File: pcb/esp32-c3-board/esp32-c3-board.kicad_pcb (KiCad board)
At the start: 2 copper layers, 118.7 x 40.6 mm, 30 parts, among them P101 CAN, P102 RS485, P3 CONN_1, P4 CONN_1, P5 CONN_1, P6 CONN_1, U102 TJA1050, U2 esp32-c3-ebay, U4 6N137, U5 DCDCConverter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

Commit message: Updated boards and readme
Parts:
- moved R3 1.20 mm to (116.1, 58.7)
- moved R4 0.81 mm to (101.1, 64.8)
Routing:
- net 3v3: track 24.9 -> 26.8 mm
- net GND: track 177.3 -> 176.3 mm
- net Net-(U4-A): track 2.93 -> 3.91 mm
- net 5V BMS: track 24.8 -> 25.6 mm
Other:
- board text added: "BMS Uart"
- board text removed: "MBS Uart"

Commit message: messed up bms uart connector
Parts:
- P102: value RS485 -> BMS UART
- R3: value 4K7 -> 2K2
- R4: value 3K3 -> 1K
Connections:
- P102 pad 2: RX from BMS -> TX to BMS
- P102 pad 3: TX to BMS -> RX from BMS
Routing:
- net Net-(U4-A): track 3.91 -> 13.7 mm
- net RX from BMS: track 22.8 -> 14.7 mm
- net 5V BMS: track 25.6 -> 31.1 mm
- net TX to BMS: track 15.7 -> 14.7 mm
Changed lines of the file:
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@@
         (effects (font (size 1 1) (thickness 0.15)))
     )
-    (fp_text value "RS485" (at 3.75 10.4 90) (layer "F.Fab")
+    (fp_text value "BMS UART" (at 3.75 10.4 90) (layer "F.Fab")
         (effects (font (size 1 1) (thickness 0.15)))
     )
@@
     (fp_line (start 9.95 9.2) (end 9.95 -2.3)
       (stroke (width 0.1) (type solid)) (layer "F.Fab"))
-    (pad "1" thru_hole roundrect (at 0 0 90) (size 2 2.5) (drill 0.95) (layers "*.Cu" "*.Mask") (roundrect_rratio 0.147059)
+    (pad "1" thru_hole roundrect (at 0 0 90) (size 2 5) (drill 0.95) (layers "*.Cu" "*.Mask") (roundrect_rratio 0.147059)
       (net 2 "GND BMS") (pinfunction "P1") (pintype "passive"))
-    (pad "2" thru_hole oval (at 2.5 0 90) (size 2 2.5) (drill 0.95) (layers "*.Cu" "*.Mask")
-      (net 14 "RX from BMS") (pinfunction "P2") (pintype "passive"))
-    (pad "3" thru_hole oval (at 5 0 90) (size 2 2.5) (drill 0.95) (layers "*.Cu" "*.Mask")
-      (net 3 "TX to BMS") (pinfunction "P3") (pintype "passive"))
-    (pad "4" thru_hole oval (at 7.5 0 90) (size 2 2.5) (drill 0.95) (layers "*.Cu" "*.Mask")
+    (pad "2" thru_hole oval (at 2.5 0 90) (size 2 5) (drill 0.95) (layers "*.Cu" "*.Mask")
+      (net 3 "TX to BMS") (pinfunction "P2") (pintype "passive"))
+    (pad "3" thru_hole oval (at 5 0 90) (size 2 5) (drill 0.95) (layers "*.Cu" "*.Mask")
+      (net 14 "RX from BMS") (pinfunction "P3") (pintype "passive"))
+    (pad "4" thru_hole oval (at 7.5 0 90) (size 2 5) (drill 0.95) (layers "*.Cu" "*.Mask")
       (net 1 "5V BMS") (pinfunction "P4") (pintype "passive"))
     (model "${KICAD6_3DMODEL_DIR}/Connector_JST.3dshapes/JST_XH_S4B-XH-A_1x04_P2.50mm_Horizontal.wrl"
@@
         (effects (font (size 1 1) (thickness 0.15)))
     )
-    (fp_text value "4K7" (at 0 1.65 90) (layer "F.Fab")
+    (fp_text value "2K2" (at 0 1.65 90) (layer "F.Fab")
         (effects (font (size 1 1) (thickness 0.15)))
     )
@@
         (effects (font (size 1 1) (thickness 0.15)))
     )
-    (fp_text value "3K3" (at 0 1.65 90) (layer "F.Fab")
+    (fp_text value "1K" (at 0 1.65 90) (layer "F.Fab")
         (effects (font (size 1 1) (thickness 0.15)))
     )
@@
   (segment (start 110.744 63.5) (end 110.0875 64.1565) (width 1) (layer "F.Cu") (net 1))
   (segment (start 112.405 63.347) (end 116.078 59.674) (width 1) (layer "F.Cu") (net 1))
-  (segment (start 118.446522 60.055) (end 120.596522 57.905) (width 1) (layer "F.Cu") (net 1))
   (segment (start 111.899416 63.51) (end 111.889416 63.5) (width 1) (layer "F.Cu") (net 1))
-  (segment (start 118.446522 60.055) (end 116.459 60.055) (width 1) (layer "F.Cu") (net 1))
   (segment (start 110.0875 64.1565) (end 110.0875 74.295) (width 1) (layer "F.Cu") (net 1))
-  (segment (start 120.596522 57.905) (end 122.555 57.905) (width 1) (layer "F.Cu") (net 1))
+  (segment (start 112.405 63.51) (end 118.01 57.905) (width 1) (layer "B.Cu") (net 1))
+  (segment (start 118.01 57.905) (end 122.555 57.905) (width 1) (layer "B.Cu") (net 1))
   (segment (start 114.935 70.8875) (end 117.0725 70.8875) (width 1) (layer "F.Cu") (net 2))
   (segment (start 114.6925 71.13) (end 114.935 70.8875) (width 1) (layer "F.Cu") (net 2))
@@
   (segment (start 112.405 71.13) (end 112.405 74.0525) (width 1) (layer "F.Cu") (net 2))
   (segment (start 112.405 68.59) (end 114.7125 68.59) (width 1) (layer "F.Cu") (net 3))
-  (segment (start 114.935 65.405) (end 119.935 60.405) (width 1) (layer "F.Cu") (net 3))
-  (segment (start 119.935 60.405) (end 122.555 60.405) (width 1) (layer "F.Cu") (net 3))
+  (segment (start 123.23 62.23) (end 122.555 62.905) (width 1) (layer "F.Cu") (net 3))
+  (segment (start 119.055 62.905) (end 114.935 67.025) (width 1) (layer "F.Cu") (net 3))
+  (segment (start 122.555 62.905) (end 119.055 62.905) (width 1) (layer "F.Cu") (net 3))
   (segment (start 114.7125 68.59) (end 114.935 68.8125) (width 1) (layer "F.Cu") (net 3))
-  (segment (start 114.935 68.8125) (end 114.935 65.405) (width 1) (layer "F.Cu") (net 3))
+  (segment (start 114.935 67.025) (end 114.935 68.8125) (width 1) (layer "F.Cu") (net 3))
   (segment (start 67.31 46.99) (end 68.81 45.49) (width 2) (layer "F.Cu") (net 4))
   (segment (start 38.8376 72.2874) (end 38.1 73.025) (width 1) (layer "F.Cu") (net 4))
@@
   (segment (start 40.145 62.23) (end 36.353 62.23) (width 1) (layer "F.Cu") (net 13))
   (segment (start 36.353 62.23) (end 34.6456 63.9374) (width 1) (layer "F.Cu") (net 13))
-  (segment (start 124.46 54.61) (end 125.095 55.245) (width 1) (layer "F.Cu") (net 14))
-  (segment (start 123.23 62.23) (end 122.555 62.905) (width 1) (layer "F.Cu") (net 14))
-  (segment (start 112.385 54.6) (end 121.91 54.6) (width 1) (layer "F.Cu") (net 14))
-  (segment (start 125.095 62.23) (end 123.23 62.23) (width 1) (layer "F.Cu") (net 14))
-  (segment (start 125.095 55.245) (end 125.095 62.23) (width 1) (layer "F.Cu") (net 14))
-  (segment (start 121.91 54.6) (end 121.92 54.61) (width 1) (layer "F.Cu") (net 14))
-  (segment (start 121.92 54.61) (end 124.46 54.61) (width 1) (layer "F.Cu") (net 14))
+  (segment (start 119.055 60.405) (end 122.555 60.405) (width 1) (layer "F.Cu") (net 14))
+  (segment (start 116.83 54.6) (end 118.11 55.88) (width 1) (layer "F.Cu") (net 14))
+  (segment (start 112.385 54.6) (end 116.83 54.6) (width 1) (layer "F.Cu") (net 14))
+  (segment (start 118.11 55.88) (end 118.11 59.46) (width 1) (layer "F.Cu") (net 14))
+  (segment (start 118.11 59.46) (end 119.055 60.405) (width 1) (layer "F.Cu") (net 14))
   (segment (start 78.63 61.595) (end 72.755 61.595) (width 1) (layer "F.Cu") (net 15))
   (segment (start 72.755 61.595) (end 68.945 65.405) (width 1) (layer "F.Cu") (net 15))
   (segment (start 68.945 65.405) (end 68.945 67.31) (width 1) (layer "F.Cu") (net 15))
   (segment (start 66.945 65.405) (end 61.53 65.405) (width 1) (layer "F.Cu") (net 16))
+  (segment (start 110.48 57.14) (end 109.982 56.642) (width 1) (layer "F.Cu") (net 17))
+  (segment (start 109.982 56.642) (end 109.982 51.308) (width 1) (layer "F.Cu") (net 17))
   (segment (start 115.544 57.14) (end 116.078 57.674) (width 1) (layer "F.Cu") (net 17))
   (segment (start 112.385 57.14) (end 115.544 57.14) (width 1) (layer "F.Cu") (net 17))
+  (segment (start 109.982 51.308) (end 111.252 50.038) (width 1) (layer "F.Cu") (net 17))
+  (segment (start 112.385 57.14) (end 110.48 57.14) (width 1) (layer "F.Cu") (net 17))
   (segment (start 101.092 65.77) (end 104.505 65.77) (width 1) (layer "F.Cu") (net 18))
   (segment (start 104.505 65.77) (end 104.785 66.05) (width 1) (layer "F.Cu") (net 18))
@@
   (segment (start 78.63 56.515) (end 79.53 56.515) (width 1) (layer "F.Cu") (net 28))
   (zone (net 4) (net_name "GND") (layers "F&B.Cu") (hatch edge 0.5)
-    (connect_pads (clearance 0.5))
-    (min_thickness 0.5) (filled_areas_thickness no)
-    (fill yes (thermal_gap 0.5) (thermal_bridge_width 0.5) (smoothing fillet) (radius 1))
+    (connect_pads yes (clearance 1))
+    (min_thickness 1) (filled_areas_thickness no)
+    (fill yes (thermal_gap 1) (thermal_bridge_width 1) (smoothing fillet) (radius 1))
     (polygon
       (pts
@@
   (zone (net 2) (net_name "GND BMS") (layers "F&B.Cu") (hatch edge 0.5)
     (priority 1)
-    (connect_pads (clearance 0.5))
+    (connect_pads yes (clearance 1))
     (min_thickness 0.5) (filled_areas_thickness no)
     (fill yes (thermal_gap 0.5) (thermal_bridge_width 0.5) (smoothing fillet) (radius 1))

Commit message: Working version connected to real BMS
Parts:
- removed C1, C4: 100nF, Capacitor_SMD:C_0805_2012Metric_Pad1.18x1.45mm_HandSolder
- removed C2, C3: 15pF, Capacitor_SMD:C_0805_2012Metric_Pad1.18x1.45mm_HandSolder
- removed R3: 2K2, Resistor_SMD:R_0805_2012Metric_Pad1.20x1.40mm_HandSolder
- removed R4: 1K, Resistor_SMD:R_0805_2012Metric_Pad1.20x1.40mm_HandSolder
- removed U6: 6N137, Package_DIP:DIP-8_W7.62mm
- added C5: 10uF, Capacitor_SMD:C_0805_2012Metric_Pad1.18x1.45mm_HandSolder, F.Cu at (112.4, 57.1)
- added C6: 10nF, Capacitor_SMD:C_0805_2012Metric_Pad1.18x1.45mm_HandSolder, F.Cu at (112.4, 55.1)
- added C7: 10uF, Capacitor_SMD:C_0805_2012Metric_Pad1.18x1.45mm_HandSolder, F.Cu at (118.1, 47.0)
- added R6: 3K3, Resistor_SMD:R_0805_2012Metric_Pad1.20x1.40mm_HandSolder, F.Cu at (115.1, 45.9)
- added R7: 10K, Resistor_SMD:R_0805_2012Metric_Pad1.20x1.40mm_HandSolder, F.Cu at (115.1, 43.4)
- added R8: 10K, Resistor_SMD:R_0805_2012Metric_Pad1.20x1.40mm_HandSolder, F.Cu at (98.6, 48.7)
- added U3: LP2985-3.3, Package_TO_SOT_SMD:SOT-23-5, F.Cu at (116.3, 51.6)
- added U7: STIS0621, Package_SO:SOIC-8_3.9x4.9mm_P1.27mm, F.Cu at (107.6, 62.9)
- U4: value 6N137 -> PC817; footprint Package_DIP:DIP-8_W7.62mm -> Package_DIP:DIP-4_W7.62mm
- moved U4 18.2 mm to (104.2, 43.5), turned to 0 degrees
- moved TH201 0.56 mm to (47.0, 53.9)
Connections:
- net Net-(D203-K) renamed 12vFused
- P102 pad 4: 5V BMS -> 12V BMS
- U4 pad 1: unconnected-(U4-NC-Pad1) -> Net-(R8-Pad1)
- U4 pad 2: Net-(U4-A) -> GND
- U4 pad 3: RX from BMS -> Net-(U3-ON/~{OFF})
- U4 pad 4: (no net) -> Net-(R7-Pad1)
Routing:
- net GND BMS: track 15.8 -> 58.3 mm, vias 0 -> 2
- net GND: track 176.3 -> 218.2 mm, vias 0 -> 1
- net 12V BMS: track 0.00 -> 31.2 mm
- net 5V BMS: track 31.1 -> 0.00 mm
- net 3v3: track 26.8 -> 9.08 mm, vias 1 -> 0
- net 3.3V BMS: track 0.00 -> 14.3 mm
- net Net-(U4-A): track 13.7 -> 0.00 mm
- net Net-(R8-Pad1): track 0.00 -> 8.12 mm
- net Net-(U3-ON/~{OFF}): track 0.00 -> 7.36 mm
- net BMS-RX: track 14.3 -> 9.46 mm
- net Net-(U3-BP): track 0.00 -> 3.96 mm
- net Net-(U6-A): track 3.81 -> 0.00 mm
- net Net-(R7-Pad1): track 0.00 -> 2.31 mm
- net TX to BMS: track 14.7 -> 12.8 mm
- net 12v: track 5.31 -> 7.06 mm
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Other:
- board text added: "BMS 0V"
- board text added: "BMS 12V"
- board text added: "RX"
- board text added: "TX"
- board text removed: "BMS Uart"

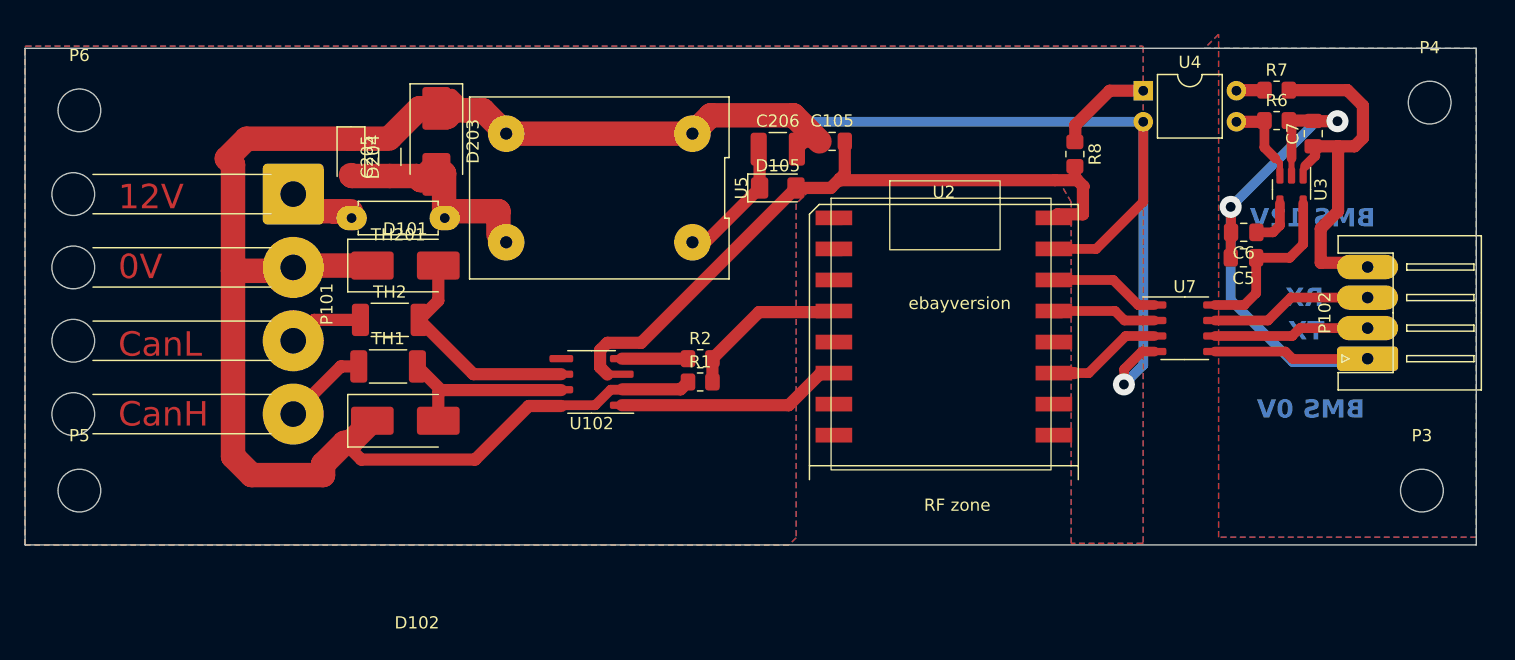
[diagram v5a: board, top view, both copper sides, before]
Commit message: Added engine Freeze frame functoinality
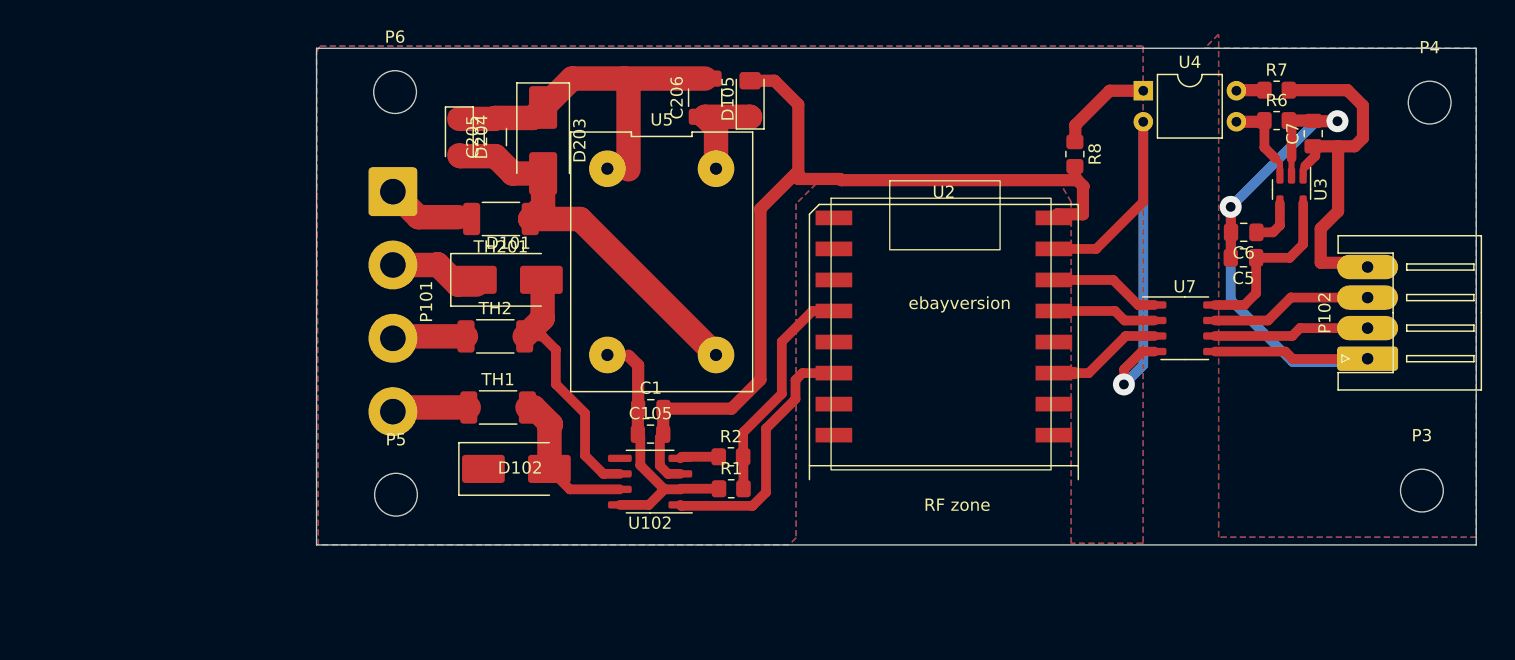
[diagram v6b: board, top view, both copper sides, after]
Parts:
- added C1: 10uF, Capacitor_SMD:C_0805_2012Metric_Pad1.18x1.45mm_HandSolder, F.Cu at (63.9, 69.5)
- P101: footprint Connector_Wire:SolderWire-1.5sqmm_1x04_P6mm_D1.7mm_OD3mm_Relief -> Connector_Wire:SolderWire-1.5sqmm_1x04_P6mm_D1.7mm_OD3mm
- R6: value 3K3 -> 10K
- R7: value 10K -> 22K
- TH201: footprint Resistor_THT:R_Axial_DIN0207_L6.3mm_D2.5mm_P7.62mm_Horizontal -> Resistor_SMD:R_2010_5025Metric_Pad1.40x2.65mm_HandSolder
- moved C105 28.2 mm to (63.9, 71.6)
- moved P5 25.9 mm to (43.1, 76.5)
- moved P6 25.9 mm to (43.0, 43.6)
- moved D102 9.91 mm to (52.9, 74.4)
- moved TH1 9.61 mm to (51.4, 69.4)
- moved U102 9.46 mm to (63.8, 75.5)
- moved R1 9.10 mm to (70.5, 76.0)
- moved D204 9.01 mm to (48.2, 47.3)
- moved C205 8.79 mm to (51.2, 47.3)
- moved TH2 8.74 mm to (51.2, 63.6)
- moved D203 8.74 mm to (55.1, 47.6)
- moved D101 8.51 mm to (52.2, 59.0)
- moved R2 8.41 mm to (70.5, 73.4)
- moved P101 8.16 mm to (42.8, 51.7)
- moved U5 7.91 mm to (64.8, 57.5), turned to -90 degrees
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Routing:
- net GND: track 218.2 -> 99.4 mm
- net 5V: track 57.1 -> 74.4 mm
- net 12vFused: track 18.9 -> 31.8 mm
- net CAN-RX: track 13.2 -> 18.7 mm
- net CAN-TX: track 18.2 -> 21.1 mm
- net Net-(D102-K): track 15.2 -> 12.6 mm
- net Net-(D101-K): track 18.6 -> 21.0 mm
- net 5.8V: track 10.5 -> 8.31 mm
- net Net-(U102-RXD): track 5.41 -> 3.19 mm
- net unconnected-(U2-gpio5-Pad1): track 0.90 -> 0.00 mm
- net unconnected-(U2-gop6-Pad2): track 0.90 -> 0.00 mm
- net 12v: track 7.06 -> 6.22 mm
- net CAN-H: track 6.97 -> 6.35 mm
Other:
- board size 118.7 x 40.6 mm -> 94.9 x 40.6 mm
- board text removed: "0V"
- board text removed: "12V"
- board text removed: "BMS 0V"
- board text removed: "BMS 12V"
- board text removed: "CanH"
- board text removed: "CanL"
- board text removed: "RX"
- board text removed: "TX"
